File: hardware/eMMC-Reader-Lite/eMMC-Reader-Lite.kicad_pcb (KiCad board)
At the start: 2 copper layers, 40.8 x 23.6 mm, 42 parts, among them J1 Conn_01x09_Socket, J2 USB_B_Mini, U2 TXS02612, U3 W25X20CLSN, U4 LM1117MP-1.8

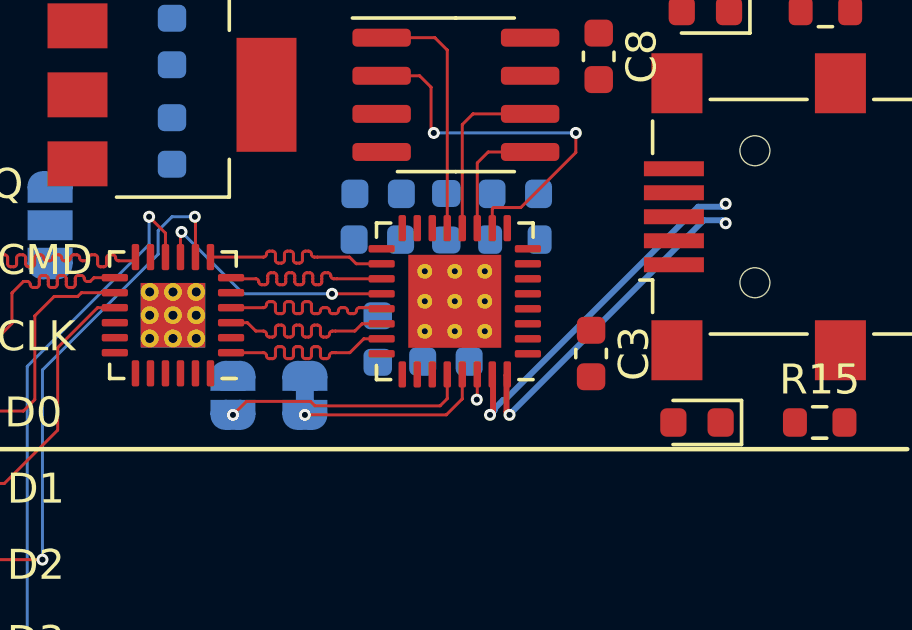
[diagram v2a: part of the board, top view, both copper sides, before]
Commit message: Fix swapped USB data lines
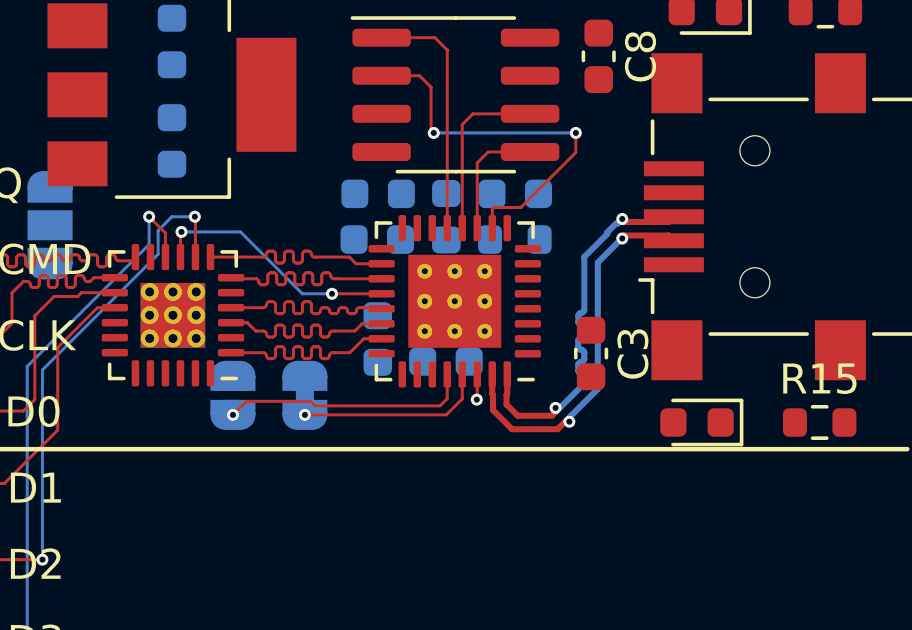
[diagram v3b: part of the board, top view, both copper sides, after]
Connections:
- U1 pad 31: /D+ -> /D-
- U1 pad 32: /D- -> /D+
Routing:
- net /D-: track 11.3 -> 12.8 mm
- net /D+: track 12.2 -> 12.8 mm
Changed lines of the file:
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@@
       (net 5 "Net-(C5-Pad1)") (pinfunction "AVDD33") (pintype "power_out"))
     (pad "31" smd roundrect (at -1.25 -2.4375 180) (size 0.25 0.875) (layers "F.Cu" "F.Paste" "F.Mask") (roundrect_rratio 0.25)
-      (net 52 "/D+") (pinfunction "D-") (pintype "bidirectional"))
+      (net 51 "/D-") (pinfunction "D-") (pintype "bidirectional"))
     (pad "32" smd roundrect (at -1.75 -2.4375 180) (size 0.25 0.875) (layers "F.Cu" "F.Paste" "F.Mask") (roundrect_rratio 0.25)
-      (net 51 "/D-") (pinfunction "D+") (pintype "bidirectional"))
+      (net 52 "/D+") (pinfunction "D+") (pintype "bidirectional"))
     (pad "33" thru_hole circle (at -1 -1 180) (size 0.5 0.5) (drill 0.2) (layers "*.Cu")
       (net 1 "GND") (pinfunction "GND") (pintype "power_out"))
@@
   (via (at 140.208 70.3865) (size 0.4) (drill 0.2) (layers "F.Cu" "B.Cu") (net 38))
   (via (at 135.191084 68.32434) (size 0.4) (drill 0.2) (layers "F.Cu" "B.Cu") (net 38))
-  (segment (start 135.191084 68.32434) (end 137.253244 70.3865) (width 0.1) (layer "B.Cu") (net 38))
-  (segment (start 137.253244 70.3865) (end 140.208 70.3865) (width 0.1) (layer "B.Cu") (net 38))
+  (segment (start 137.15834 68.32434) (end 139.2205 70.3865) (width 0.1) (layer "B.Cu") (net 38))
+  (segment (start 139.2205 70.3865) (end 140.208 70.3865) (width 0.1) (layer "B.Cu") (net 38))
+  (segment (start 135.191084 68.32434) (end 137.15834 68.32434) (width 0.1) (layer "B.Cu") (net 38))
   (segment (start 139.622 71.05) (end 139.722 71.05) (width 0.1) (layer "F.Cu") (net 39))
   (segment (start 138.122 70.65) (end 138.222 70.65) (width 0.1) (layer "F.Cu") (net 39))
@@
   (segment (start 144.55 73.074) (end 144.55 73.89) (width 0.1) (layer "F.Cu") (net 49))
   (via (at 139.304001 74.422) (size 0.4) (drill 0.2) (layers "F.Cu" "B.Cu") (net 49))
-  (segment (start 146.025001 74.322001) (end 146.125 74.422) (width 0.2) (layer "F.Cu") (net 51))
-  (segment (start 146.05 73.074) (end 146.025001 73.098999) (width 0.2) (layer "F.Cu") (net 51))
-  (segment (start 146.025001 73.098999) (end 146.025001 74.322001) (width 0.2) (layer "F.Cu") (net 51))
-  (via (at 146.125 74.422) (size 0.4) (drill 0.2) (layers "F.Cu" "B.Cu") (net 51))
-  (via (at 153.329438 68.035) (size 0.4) (drill 0.2) (layers "F.Cu" "B.Cu") (net 51))
-  (segment (start 146.125 74.422) (end 146.125 74.408397) (width 0.2) (layer "B.Cu") (net 51))
-  (segment (start 153.229439 67.935001) (end 153.329438 68.035) (width 0.2) (layer "B.Cu") (net 51))
-  (segment (start 152.598396 67.935001) (end 153.229439 67.935001) (width 0.2) (layer "B.Cu") (net 51))
-  (segment (start 146.125 74.408397) (end 152.598396 67.935001) (width 0.2) (layer "B.Cu") (net 51))
-  (segment (start 145.574999 73.098999) (end 145.574999 74.322001) (width 0.2) (layer "F.Cu") (net 52))
-  (segment (start 145.55 73.074) (end 145.574999 73.098999) (width 0.2) (layer "F.Cu") (net 52))
-  (segment (start 145.574999 74.322001) (end 145.475 74.422) (width 0.2) (layer "F.Cu") (net 52))
-  (via (at 153.329438 67.385) (size 0.4) (drill 0.2) (layers "F.Cu" "B.Cu") (net 52))
-  (via (at 145.475 74.422) (size 0.4) (drill 0.2) (layers "F.Cu" "B.Cu") (net 52))
-  (segment (start 145.475 74.422) (end 145.625 74.272) (width 0.2) (layer "B.Cu") (net 52))
-  (segment (start 145.625 74.214893) (end 145.917893 73.922) (width 0.2) (layer "B.Cu") (net 52))
-  (segment (start 153.229439 67.484999) (end 153.329438 67.385) (width 0.2) (layer "B.Cu") (net 52))
-  (segment (start 145.625 74.272) (end 145.625 74.214893) (width 0.2) (layer "B.Cu") (net 52))
-  (segment (start 152.412001 67.484999) (end 153.229439 67.484999) (width 0.2) (layer "B.Cu") (net 52))
-  (segment (start 145.975 73.922) (end 152.412001 67.484999) (width 0.2) (layer "B.Cu") (net 52))
-  (segment (start 145.917893 73.922) (end 145.975 73.922) (width 0.2) (layer "B.Cu") (net 52))
+  (segment (start 147.726747 74.901) (end 147.978293 74.649454) (width 0.2) (layer "F.Cu") (net 51))
+  (segment (start 151.605 68.618) (end 151.430001 68.443001) (width 0.2) (layer "F.Cu") (net 51))
+  (segment (start 151.430001 68.443001) (end 149.983134 68.443001) (width 0.2) (layer "F.Cu") (net 51))
+  (segment (start 147.978293 74.649454) (end 148.119714 74.649454) (width 0.2) (layer "F.Cu") (net 51))
+  (segment (start 145.575 73.755251) (end 145.575 74.2652) (width 0.2) (layer "F.Cu") (net 51))
+  (segment (start 145.55 73.730251) (end 145.575 73.755251) (width 0.2) (layer "F.Cu") (net 51))
+  (segment (start 145.55 73.074) (end 145.55 73.730251) (width 0.2) (layer "F.Cu") (net 51))
+  (segment (start 146.2108 74.901) (end 147.726747 74.901) (width 0.2) (layer "F.Cu") (net 51))
+  (segment (start 149.983134 68.443001) (end 149.883135 68.543) (width 0.2) (layer "F.Cu") (net 51))
+  (segment (start 145.575 74.2652) (end 146.2108 74.901) (width 0.2) (layer "F.Cu") (net 51))
+  (via (at 149.883135 68.543) (size 0.4) (drill 0.2) (layers "F.Cu" "B.Cu") (net 51))
+  (via (at 148.119714 74.649454) (size 0.4) (drill 0.2) (layers "F.Cu" "B.Cu") (net 51))
+  (segment (start 148.119714 74.508033) (end 149.069 73.558747) (width 0.2) (layer "B.Cu") (net 51))
+  (segment (start 148.119714 74.649454) (end 148.119714 74.508033) (width 0.2) (layer "B.Cu") (net 51))
+  (segment (start 149.869532 68.543) (end 149.883135 68.543) (width 0.2) (layer "B.Cu") (net 51))
+  (segment (start 149.069 73.558747) (end 149.069 69.343532) (width 0.2) (layer "B.Cu") (net 51))
+  (segment (start 149.069 69.343532) (end 149.869532 68.543) (width 0.2) (layer "B.Cu") (net 51))
+  (segment (start 146.05 73.730251) (end 146.025 73.755251) (width 0.2) (layer "F.Cu") (net 52))
+  (segment (start 147.540349 74.451) (end 147.660094 74.331255) (width 0.2) (layer "F.Cu") (net 52))
+  (segment (start 146.025 74.0788) (end 146.3972 74.451) (width 0.2) (layer "F.Cu") (net 52))
+  (segment (start 151.605 67.818) (end 151.430001 67.992999) (width 0.2) (layer "F.Cu") (net 52))
+  (segment (start 149.983134 67.992999) (end 149.883135 67.893) (width 0.2) (layer "F.Cu") (net 52))
+  (segment (start 147.660094 74.331255) (end 147.660094 74.189834) (width 0.2) (layer "F.Cu") (net 52))
+  (segment (start 146.025 73.755251) (end 146.025 74.0788) (width 0.2) (layer "F.Cu") (net 52))
+  (segment (start 146.3972 74.451) (end 147.540349 74.451) (width 0.2) (layer "F.Cu") (net 52))
+  (segment (start 146.05 73.074) (end 146.05 73.730251) (width 0.2) (layer "F.Cu") (net 52))
+  (segment (start 151.430001 67.992999) (end 149.983134 67.992999) (width 0.2) (layer "F.Cu") (net 52))
+  (via (at 149.883135 67.893) (size 0.4) (drill 0.2) (layers "F.Cu" "B.Cu") (net 52))
+  (via (at 147.660094 74.189834) (size 0.4) (drill 0.2) (layers "F.Cu" "B.Cu") (net 52))
+  (segment (start 148.419 72.952) (end 148.419 72.752) (width 0.2) (layer "B.Cu") (net 52))
+  (segment (start 149.676028 68.043) (end 149.733135 68.043) (width 0.2) (layer "B.Cu") (net 52))
+  (segment (start 148.62 70.92) (end 148.62 69.158135) (width 0.2) (layer "B.Cu") (net 52))
+  (segment (start 149.383135 68.393) (end 149.383135 68.335893) (width 0.2) (layer "B.Cu") (net 52))
+  (segment (start 147.660094 74.189834) (end 147.801515 74.189834) (width 0.2) (layer "B.Cu") (net 52))
+  (segment (start 149.383135 68.335893) (end 149.676028 68.043) (width 0.2) (layer "B.Cu") (net 52))
+  (segment (start 148.619 69.157135) (end 149.383135 68.393) (width 0.2) (layer "B.Cu") (net 52))
+  (segment (start 148.619 73.372349) (end 148.619 73.152) (width 0.2) (layer "B.Cu") (net 52))
+  (segment (start 149.733135 68.043) (end 149.883135 67.893) (width 0.2) (layer "B.Cu") (net 52))
+  (segment (start 148.62 71.52) (end 148.619 71.521) (width 0.2) (layer "B.Cu") (net 52))
+  (segment (start 148.419 72.152) (end 148.419 71.952) (width 0.2) (layer "B.Cu") (net 52))
+  (segment (start 148.619 72.552) (end 148.619 72.352) (width 0.2) (layer "B.Cu") (net 52))
+  (segment (start 147.801515 74.189834) (end 148.619 73.372349) (width 0.2) (layer "B.Cu") (net 52))
+  (segment (start 148.619 71.521) (end 148.619 71.752) (width 0.2) (layer "B.Cu") (net 52))
+  (segment (start 148.62 69.158135) (end 148.619 69.157135) (width 0.2) (layer "B.Cu") (net 52))
+  (segment (start 148.42 71.32) (end 148.42 71.12) (width 0.2) (layer "B.Cu") (net 52))
+  (arc (start 148.419 72.752) (mid 148.448289 72.681289) (end 148.519 72.652) (width 0.2) (layer "B.Cu") (net 52))
+  (arc (start 148.62 71.52) (mid 148.590711 71.449289) (end 148.52 71.42) (width 0.2) (layer "B.Cu") (net 52))
+  (arc (start 148.52 71.02) (mid 148.590711 70.990711) (end 148.62 70.92) (width 0.2) (layer "B.Cu") (net 52))
+  (arc (start 148.519 72.252) (mid 148.448289 72.222711) (end 148.419 72.152) (width 0.2) (layer "B.Cu") (net 52))
+  (arc (start 148.619 73.152) (mid 148.589711 73.081289) (end 148.519 73.052) (width 0.2) (layer "B.Cu") (net 52))
+  (arc (start 148.519 72.652) (mid 148.589711 72.622711) (end 148.619 72.552) (width 0.2) (layer "B.Cu") (net 52))
+  (arc (start 148.519 71.852) (mid 148.589711 71.822711) (end 148.619 71.752) (width 0.2) (layer "B.Cu") (net 52))
+  (arc (start 148.419 71.952) (mid 148.448289 71.881289) (end 148.519 71.852) (width 0.2) (layer "B.Cu") (net 52))
+  (arc (start 148.619 72.352) (mid 148.589711 72.281289) (end 148.519 72.252) (width 0.2) (layer "B.Cu") (net 52))
+  (arc (start 148.42 71.12) (mid 148.449289 71.049289) (end 148.52 71.02) (width 0.2) (layer "B.Cu") (net 52))
+  (arc (start 148.52 71.42) (mid 148.449289 71.390711) (end 148.42 71.32) (width 0.2) (layer "B.Cu") (net 52))
+  (arc (start 148.519 73.052) (mid 148.448289 73.022711) (end 148.419 72.952) (width 0.2) (layer "B.Cu") (net 52))
 )

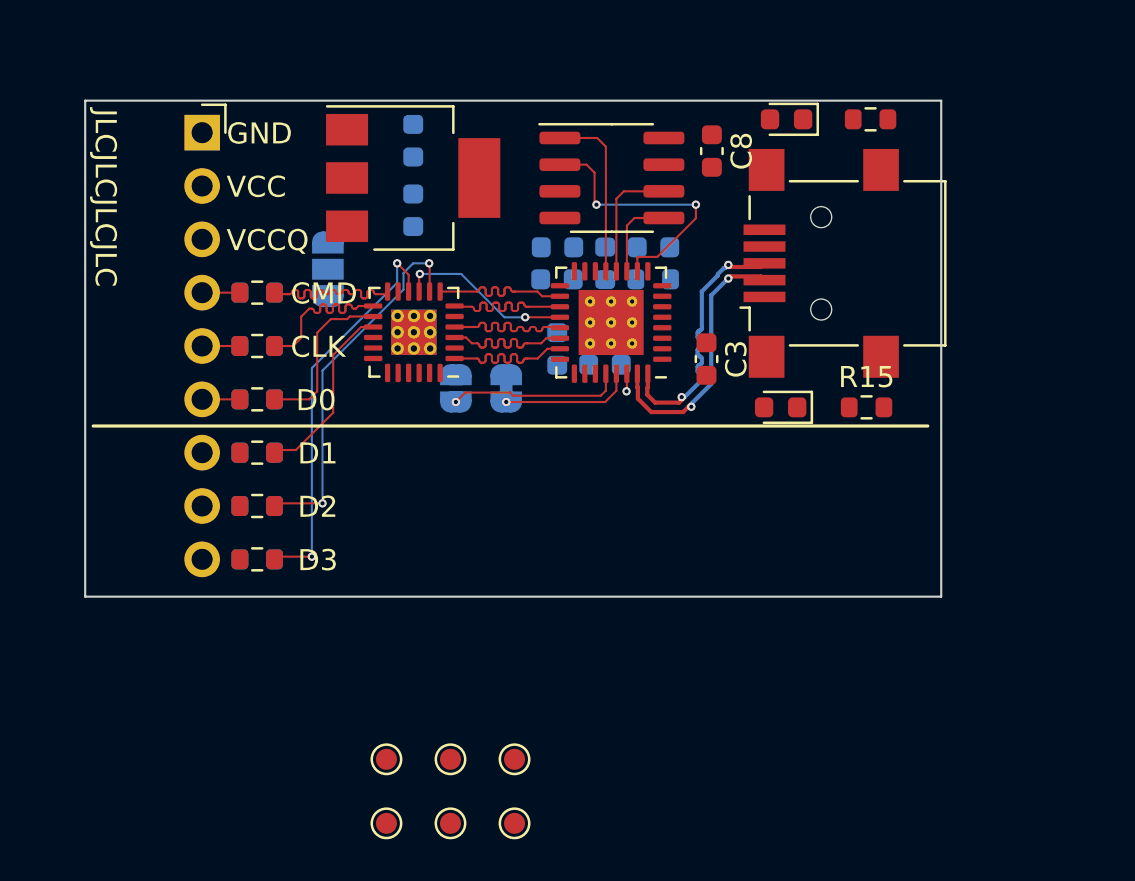
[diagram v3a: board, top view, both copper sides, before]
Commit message: Basic routing (needs properly-sized traces, cleaner copper pours)
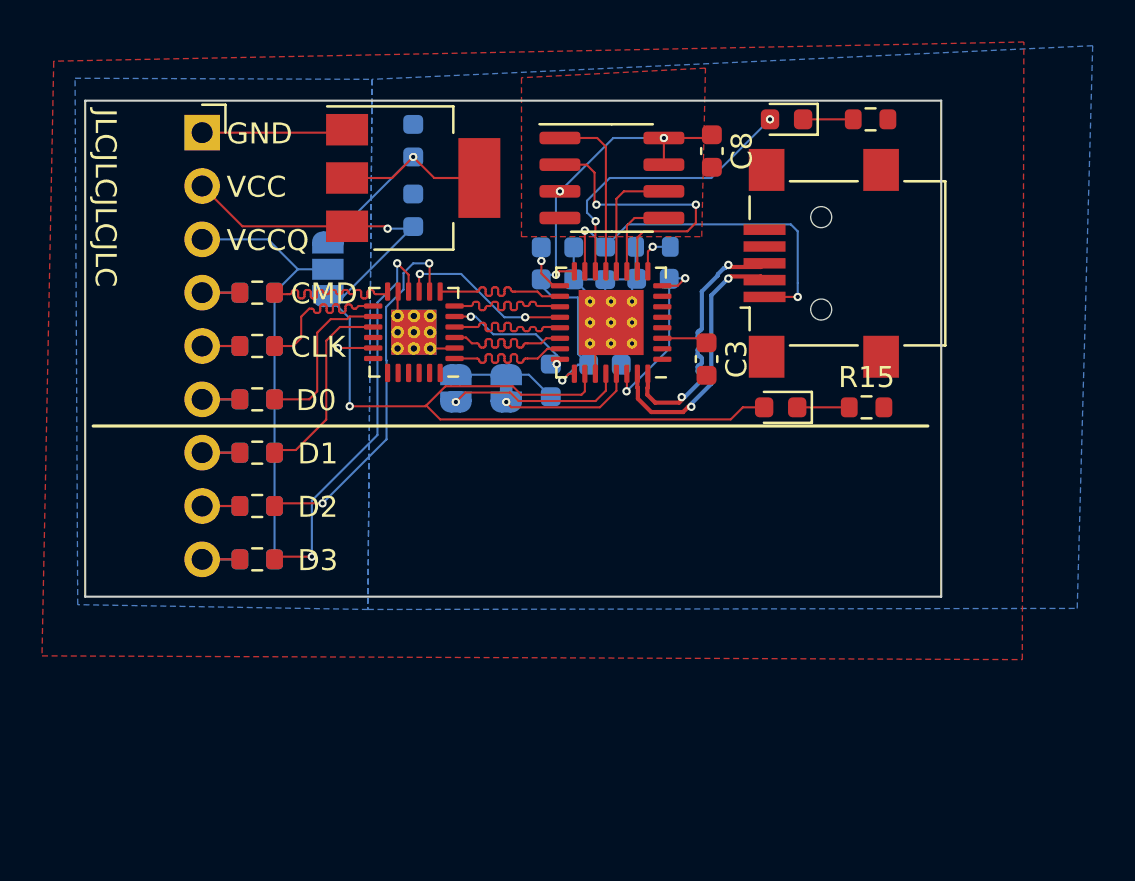
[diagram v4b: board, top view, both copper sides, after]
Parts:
- removed TP1, TP2, TP3, TP4, TP5, TP6: TestPoint_Small, TestPoint:TestPoint_Pad_D1.0mm
- moved R14 1.55 mm to (146.3, 67.0)
- moved C1 1.53 mm to (141.4, 73.4), turned to -90 degrees
- moved C4 1.52 mm to (141.7, 67.1)
- moved C6 1.52 mm to (141.7, 68.6), turned to 0 degrees
- moved C5 1.50 mm to (146.3, 68.6)
- turned JP3 to -90 degrees
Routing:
- net /SD_VCC: track 0.00 -> 51.4 mm, vias 0 -> 2
- net GND: track 0.00 -> 29.0 mm
- net +3V3: track 0.00 -> 23.4 mm, vias 0 -> 4
- net VCCQ: track 0.00 -> 22.5 mm, vias 0 -> 1
- net VBUS: track 0.00 -> 17.7 mm, vias 0 -> 2
- net Net-(D1-A): track 0.00 -> 13.9 mm, vias 0 -> 2
- net +1V8: track 0.00 -> 12.9 mm, vias 0 -> 1
- net Net-(C5-Pad1): track 0.85 -> 9.53 mm, vias 1 -> 2
- net /VCCA: track 0.00 -> 6.35 mm, vias 0 -> 2
- net Net-(J1-Pin_9): track 0.00 -> 3.59 mm
- net Net-(J1-Pin_8): track 0.00 -> 3.59 mm
- net Net-(J1-Pin_7): track 0.00 -> 3.59 mm
- net Net-(D2-K): track 0.00 -> 2.48 mm
- net Net-(D1-K): track 0.00 -> 2.39 mm
- net Net-(U1C-DVDD12): track 0.00 -> 2.38 mm, vias 0 -> 1
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- added copper zone on F.Cu, net +3V3
- added copper zone on B.Cu, net GND
- added copper zone on F.Cu, net GND
- added copper zone on B.Cu, net VCCQ
